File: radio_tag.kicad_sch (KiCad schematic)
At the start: 20 parts, among them J1 Conn_01x01, J2 Conn_01x01, J3 Conn_01x01, U1 TLV740P, U2 MICRF113, Y1 13M560

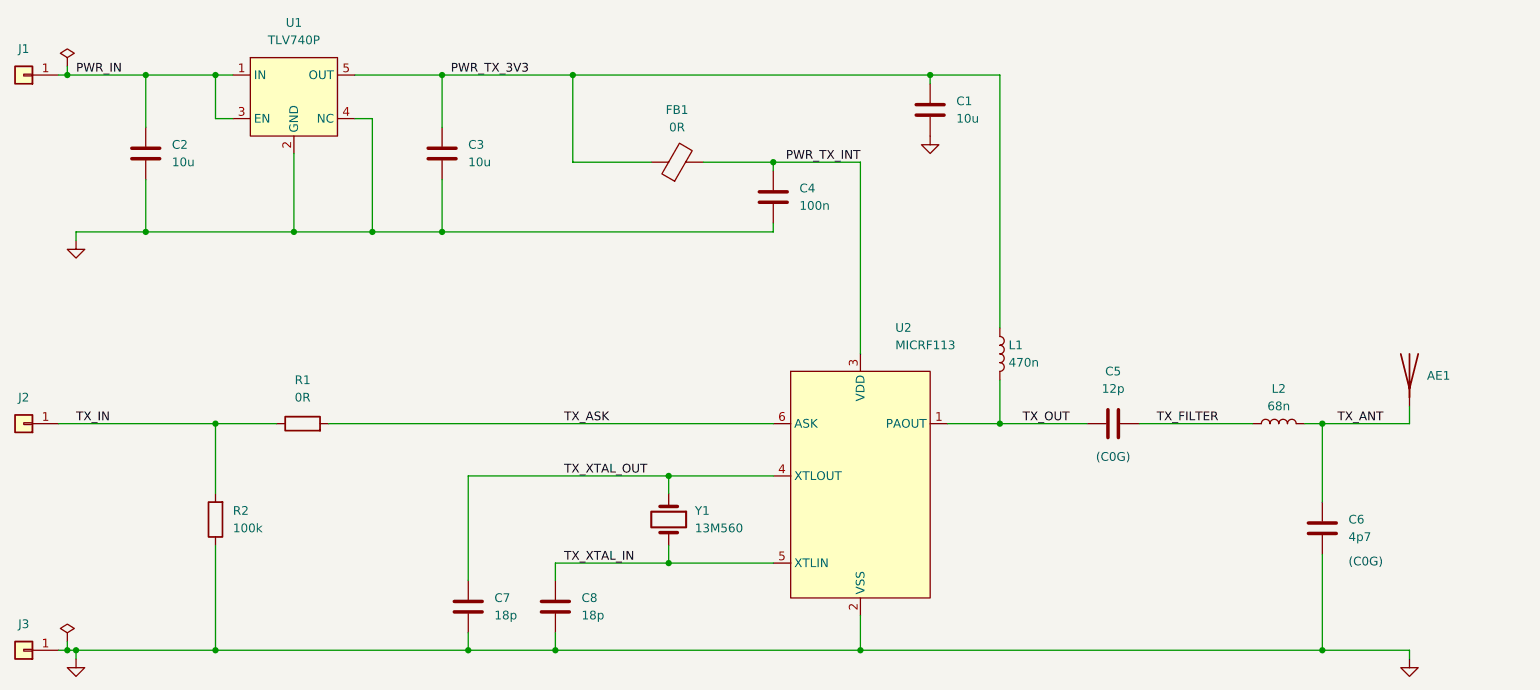
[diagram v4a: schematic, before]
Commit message: Revise board to use SMA edge mount connector, mark as Rev. B
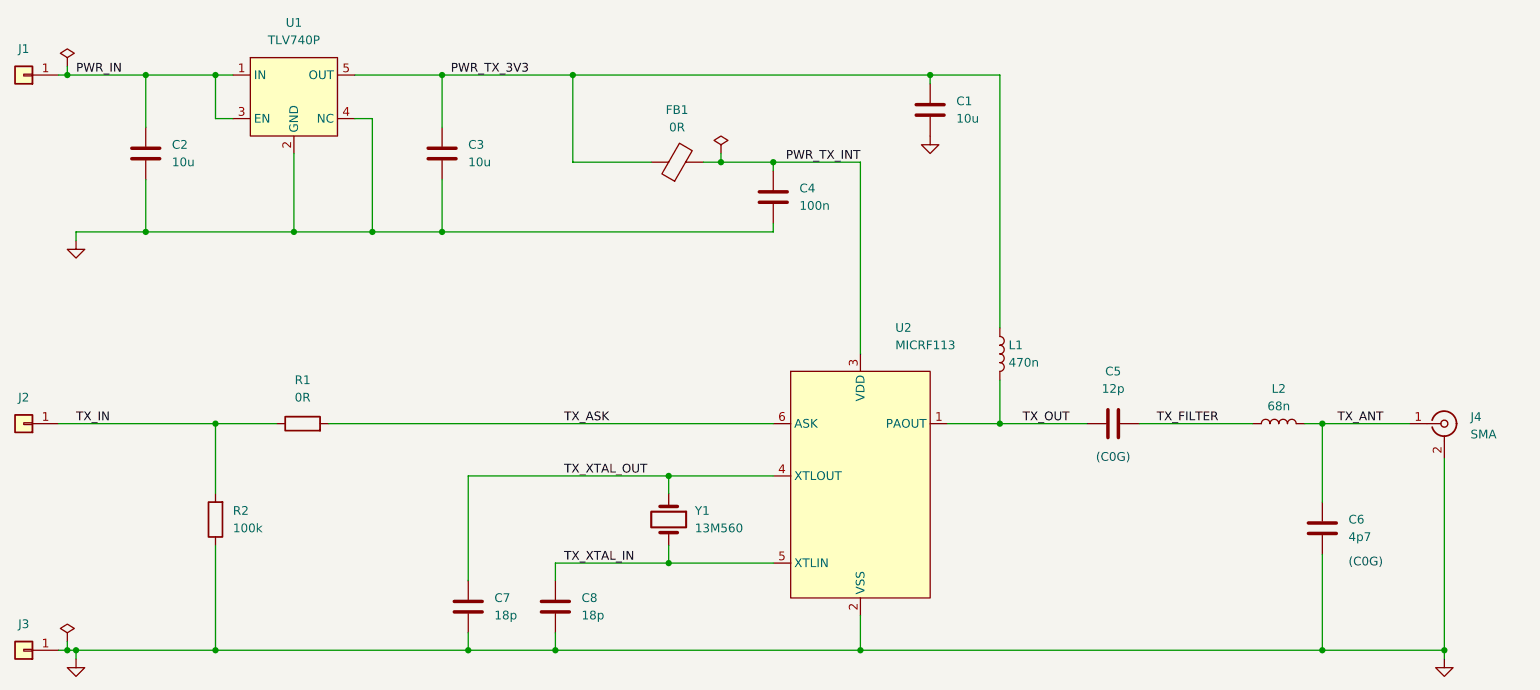
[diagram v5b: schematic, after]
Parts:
- removed AE1: Antenna_Dipole, rf:TE_ANT-433-HETH, symbol Device:Antenna
- added J4: SMA, Connector_Coaxial:SMA_Samtec_SMA-J-P-H-ST-EM1_EdgeMount, symbol Connector:Conn_Coaxial
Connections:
- net GND: now also J4.2 (Ext)
- net TX_ANT: now also J4.1 (In)
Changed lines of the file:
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@@
 	(title_block
 		(title "ASK Radio Development Board")
+		(date "2025-02-02")
+		(rev "B")
 		(company "J. L. Hay")
 	)
@@
 	)
 	(junction
+		(at 250.19 133.35)
+		(diameter 0)
+		(color 0 0 0 0)
+	)
+	(junction
 		(at 82.55 72.39)
 		(diameter 0)
@@
 	)
 	(junction
+		(at 144.78 62.23)
+		(diameter 0)
+		(color 0 0 0 0)
+	)
+	(junction
 		(at 137.16 107.95)
 		(diameter 0)
@@
 	(wire
 		(pts
-			(xy 245.11 134.62) (xy 245.11 133.35)
+			(xy 250.19 134.62) (xy 250.19 133.35)
 		)
 		(stroke
@@
 	(wire
 		(pts
+			(xy 144.78 62.23) (xy 152.4 62.23)
+		)
+		(stroke
+			(width 0)
+			(type default)
+		)
+	)
+	(wire
+		(pts
 			(xy 137.16 120.65) (xy 137.16 118.11)
 		)
@@
 	(wire
 		(pts
-			(xy 91.44 49.53) (xy 104.14 49.53)
+			(xy 71.12 133.35) (xy 107.95 133.35)
 		)
 		(stroke
@@
 	(wire
 		(pts
-			(xy 245.11 97.79) (xy 245.11 100.33)
+			(xy 250.19 105.41) (xy 250.19 133.35)
 		)
 		(stroke
@@
 	(wire
 		(pts
-			(xy 71.12 133.35) (xy 107.95 133.35)
+			(xy 185.42 100.33) (xy 198.12 100.33)
 		)
 		(stroke
@@
 	(wire
 		(pts
-			(xy 185.42 100.33) (xy 198.12 100.33)
+			(xy 104.14 72.39) (xy 152.4 72.39)
 		)
 		(stroke
@@
 	(wire
 		(pts
-			(xy 104.14 72.39) (xy 152.4 72.39)
+			(xy 107.95 107.95) (xy 137.16 107.95)
 		)
 		(stroke
@@
 	(wire
 		(pts
-			(xy 107.95 107.95) (xy 137.16 107.95)
+			(xy 137.16 120.65) (xy 152.4 120.65)
 		)
 		(stroke
@@
 	(wire
 		(pts
-			(xy 137.16 120.65) (xy 152.4 120.65)
+			(xy 177.8 100.33) (xy 185.42 100.33)
 		)
 		(stroke
@@
 	(wire
 		(pts
-			(xy 177.8 100.33) (xy 185.42 100.33)
+			(xy 87.63 100.33) (xy 152.4 100.33)
 		)
 		(stroke
@@
 	(wire
 		(pts
-			(xy 87.63 100.33) (xy 152.4 100.33)
+			(xy 165.1 128.27) (xy 165.1 133.35)
 		)
 		(stroke
@@
 	(wire
 		(pts
-			(xy 165.1 128.27) (xy 165.1 133.35)
+			(xy 144.78 60.96) (xy 144.78 62.23)
 		)
 		(stroke
@@
 	(wire
 		(pts
+			(xy 91.44 49.53) (xy 104.14 49.53)
+		)
+		(stroke
+			(width 0)
+			(type default)
+		)
+	)
+	(wire
+		(pts
 			(xy 48.26 133.35) (xy 49.53 133.35)
 		)
@@
 	(wire
 		(pts
-			(xy 142.24 62.23) (xy 152.4 62.23)
+			(xy 142.24 62.23) (xy 144.78 62.23)
 		)
 		(stroke
@@
 	(wire
 		(pts
-			(xy 232.41 133.35) (xy 245.11 133.35)
+			(xy 232.41 133.35) (xy 250.19 133.35)
 		)
 		(stroke
@@
 	)
 	(symbol
+		(lib_id "Connector:Conn_Coaxial")
+		(at 250.19 100.33 0)
+		(unit 1)
+		(exclude_from_sim no)
+		(in_bom yes)
+		(on_board yes)
+		(dnp no)
+		(fields_autoplaced yes)
+		(property "Reference" "J4"
+			(at 254 99.3531 0)
+			(effects
+				(font
+					(size 1.27 1.27)
+				)
+				(justify left)
+			)
+		)
+		(property "Value" "SMA"
+			(at 254 101.8931 0)
+			(effects
+				(font
+					(size 1.27 1.27)
+				)
+				(justify left)
+			)
+		)
+		(property "Footprint" "Connector_Coaxial:SMA_Samtec_SMA-J-P-H-ST-EM1_EdgeMount"
+			(at 250.19 100.33 0)
+			(effects
+				(font
+					(size 1.27 1.27)
+				)
+				(hide yes)
+			)
+		)
+		(property "Datasheet" "https://www.rfsolutions.co.uk/content/download-files/CON-SMA-EDGE-6-DATASHEET.pdf"
+			(at 250.19 100.33 0)
+			(effects
+				(font
+					(size 1.27 1.27)
+				)
+				(hide yes)
+			)
+		)
+		(property "Description" "coaxial connector (BNC, SMA, SMB, SMC, Cinch/RCA, LEMO, ...)"
+			(at 250.19 100.33 0)
+			(effects
+				(font
+					(size 1.27 1.27)
+				)
+				(hide yes)
+			)
+		)
+		(property "Manufacturer" "RF Solutions"
+			(at 250.19 100.33 0)
+			(effects
+				(font
+					(size 1.27 1.27)
+				)
+				(hide yes)
+			)
+		)
+		(property "Manufacturer PN" "CON-SMA-EDGE-S"
+			(at 250.19 100.33 0)
+			(effects
+				(font
+					(size 1.27 1.27)
+				)
+				(hide yes)
+			)
+		)
+		(property "Supplier" "Digi-Key"
+			(at 250.19 100.33 0)
+			(effects
+				(font
+					(size 1.27 1.27)
+				)
+				(hide yes)
+			)
+		)
+		(property "Supplier PN" "CON-SMA-EDGE-S-ND"
+			(at 250.19 100.33 0)
+			(effects
+				(font
+					(size 1.27 1.27)
+				)
+				(hide yes)
+			)
+		)
+		(pin "2"
+		)
+		(pin "1"
+		)
+		(instances
+			(project ""
+				(path "/370f7c37-aff5-4805-bec3-2aecd31a4468"
+					(reference "J4")
+					(unit 1)
+				)
+			)
+		)
+	)
+	(symbol
 		(lib_id "Device:FerriteBead")
 		(at 138.43 62.23 90)
@@
 	(symbol
 		(lib_id "power:GND")
-		(at 245.11 134.62 0)
+		(at 250.19 134.62 0)
 		(unit 1)
 		(exclude_from_sim no)
@@
 		(fields_autoplaced yes)
 		(property "Reference" "#PWR04"
-			(at 245.11 140.97 0)
+			(at 250.19 140.97 0)
 			(effects
 				(font
@@
 		)
 		(property "Value" "GND"
-			(at 245.11 139.7 0)
+			(at 250.19 139.7 0)
 			(effects
 				(font
@@
 		)
 		(property "Footprint" ""
-			(at 245.11 134.62 0)
+			(at 250.19 134.62 0)
 			(effects
 				(font
@@
 		)
 		(property "Datasheet" ""
-			(at 245.11 134.62 0)
+			(at 250.19 134.62 0)
 			(effects
 				(font
@@
 		)
 		(property "Description" "Power symbol creates a global label with name \"GND\" , ground"
-			(at 245.11 134.62 0)
+			(at 250.19 134.62 0)
 			(effects
 				(font
@@
 	)
 	(symbol
+		(lib_id "power:PWR_FLAG")
+		(at 144.78 60.96 0)
+		(unit 1)
+		(exclude_from_sim no)
+		(in_bom yes)
+		(on_board yes)
+		(dnp no)
+		(fields_autoplaced yes)
+		(property "Reference" "#FLG03"
+			(at 144.78 59.055 0)
+			(effects
+				(font
+					(size 1.27 1.27)
+				)
+				(hide yes)
+			)
+		)
+		(property "Value" "PWR_FLAG"
+			(at 144.78 55.88 0)
+			(effects
+				(font
+					(size 1.27 1.27)
+				)
+				(hide yes)
+			)
+		)
+		(property "Footprint" ""
+			(at 144.78 60.96 0)
+			(effects
+				(font
+					(size 1.27 1.27)
+				)
+				(hide yes)
+			)
+		)
+		(property "Datasheet" "~"
+			(at 144.78 60.96 0)
+			(effects
+				(font
+					(size 1.27 1.27)
+				)
+				(hide yes)
+			)
+		)
+		(property "Description" "Special symbol for telling ERC where power comes from"
+			(at 144.78 60.96 0)
+			(effects
+				(font
+					(size 1.27 1.27)
+				)
+				(hide yes)
+			)
+		)
+		(pin "1"
+		)
+		(instances
+			(project "radio_tag"
+				(path "/370f7c37-aff5-4805-bec3-2aecd31a4468"
+					(reference "#FLG03")
+					(unit 1)
+				)
+			)
+		)
+	)
+	(symbol
 		(lib_id "Connector_Generic:Conn_01x01")
 		(at 43.18 100.33 180)
@@
 					(unit 1)
 				)
-			)
-		)
-	)
-	(symbol
-		(lib_id "Device:Antenna")
-		(at 245.11 92.71 0)
-		(unit 1)
-		(exclude_from_sim no)
-		(in_bom yes)
-		(on_board yes)
-		(dnp no)
-		(fields_autoplaced yes)
-		(property "Reference" "AE1"
-			(at 247.65 93.3449 0)
-			(effects
-				(font
-					(size 1.27 1.27)
-				)
-				(justify left)
-			)
-		)
-		(property "Value" "Antenna_Dipole"
-			(at 247.6499 92.71 90)
-			(effects
-				(font
-					(size 1.27 1.27)
-				)
-				(justify left)
-				(hide yes)
-			)
-		)
-		(property "Footprint" "rf:TE_ANT-433-HETH"
-			(at 245.11 92.71 0)
-			(effects
-				(font
-					(size 1.27 1.27)
-				)
-				(hide yes)
-			)
-		)
-		(property "Datasheet" "~"
-			(at 245.11 92.71 0)
-			(effects
-				(font
-					(size 1.27 1.27)
-				)
-				(hide yes)
-			)
-		)
-		(property "Description" "Antenna"
-			(at 245.11 92.71 0)
-			(effects
-				(font
-					(size 1.27 1.27)
-				)
-				(hide yes)
-			)
-		)
-		(property "Supplier " "Digi-Key"
-			(at 245.11 92.71 0)
-			(effects
-				(font
-					(size 1.27 1.27)
-				)
-				(hide yes)
-			)
-		)
-		(property "Manufacturer" "TE Connectivity"
-			(at 245.11 92.71 0)
-			(effects
-				(font
-					(size 1.27 1.27)
-				)
-				(hide yes)
-			)
-		)
-		(property "Manufacturer PN" "ANT-433-HETH"
-			(at 245.11 92.71 0)
-			(effects
-				(font
-					(size 1.27 1.27)
-				)
-				(hide yes)
-			)
-		)
-		(property "Supplier PN" "ANT-433-HETH-ND"
-			(at 245.11 92.71 0)
-			(effects
-				(font
-					(size 1.27 1.27)
-				)
-				(hide yes)
-			)
-		)
-		(pin "1"
-		)
-		(instances
-			(project ""
-				(path "/370f7c37-aff5-4805-bec3-2aecd31a4468"
-					(reference "AE1")
-					(unit 1)
-				)
